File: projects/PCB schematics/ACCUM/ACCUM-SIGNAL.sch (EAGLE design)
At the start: 31 parts, among them IC1 OPA454, J1 2P_1-770166-0, J2 2P_1-770166-0, J3 2P_1-770166-0, J4 2P_1-770166-0, Q1 IRLZ44Z, X1 5566-2

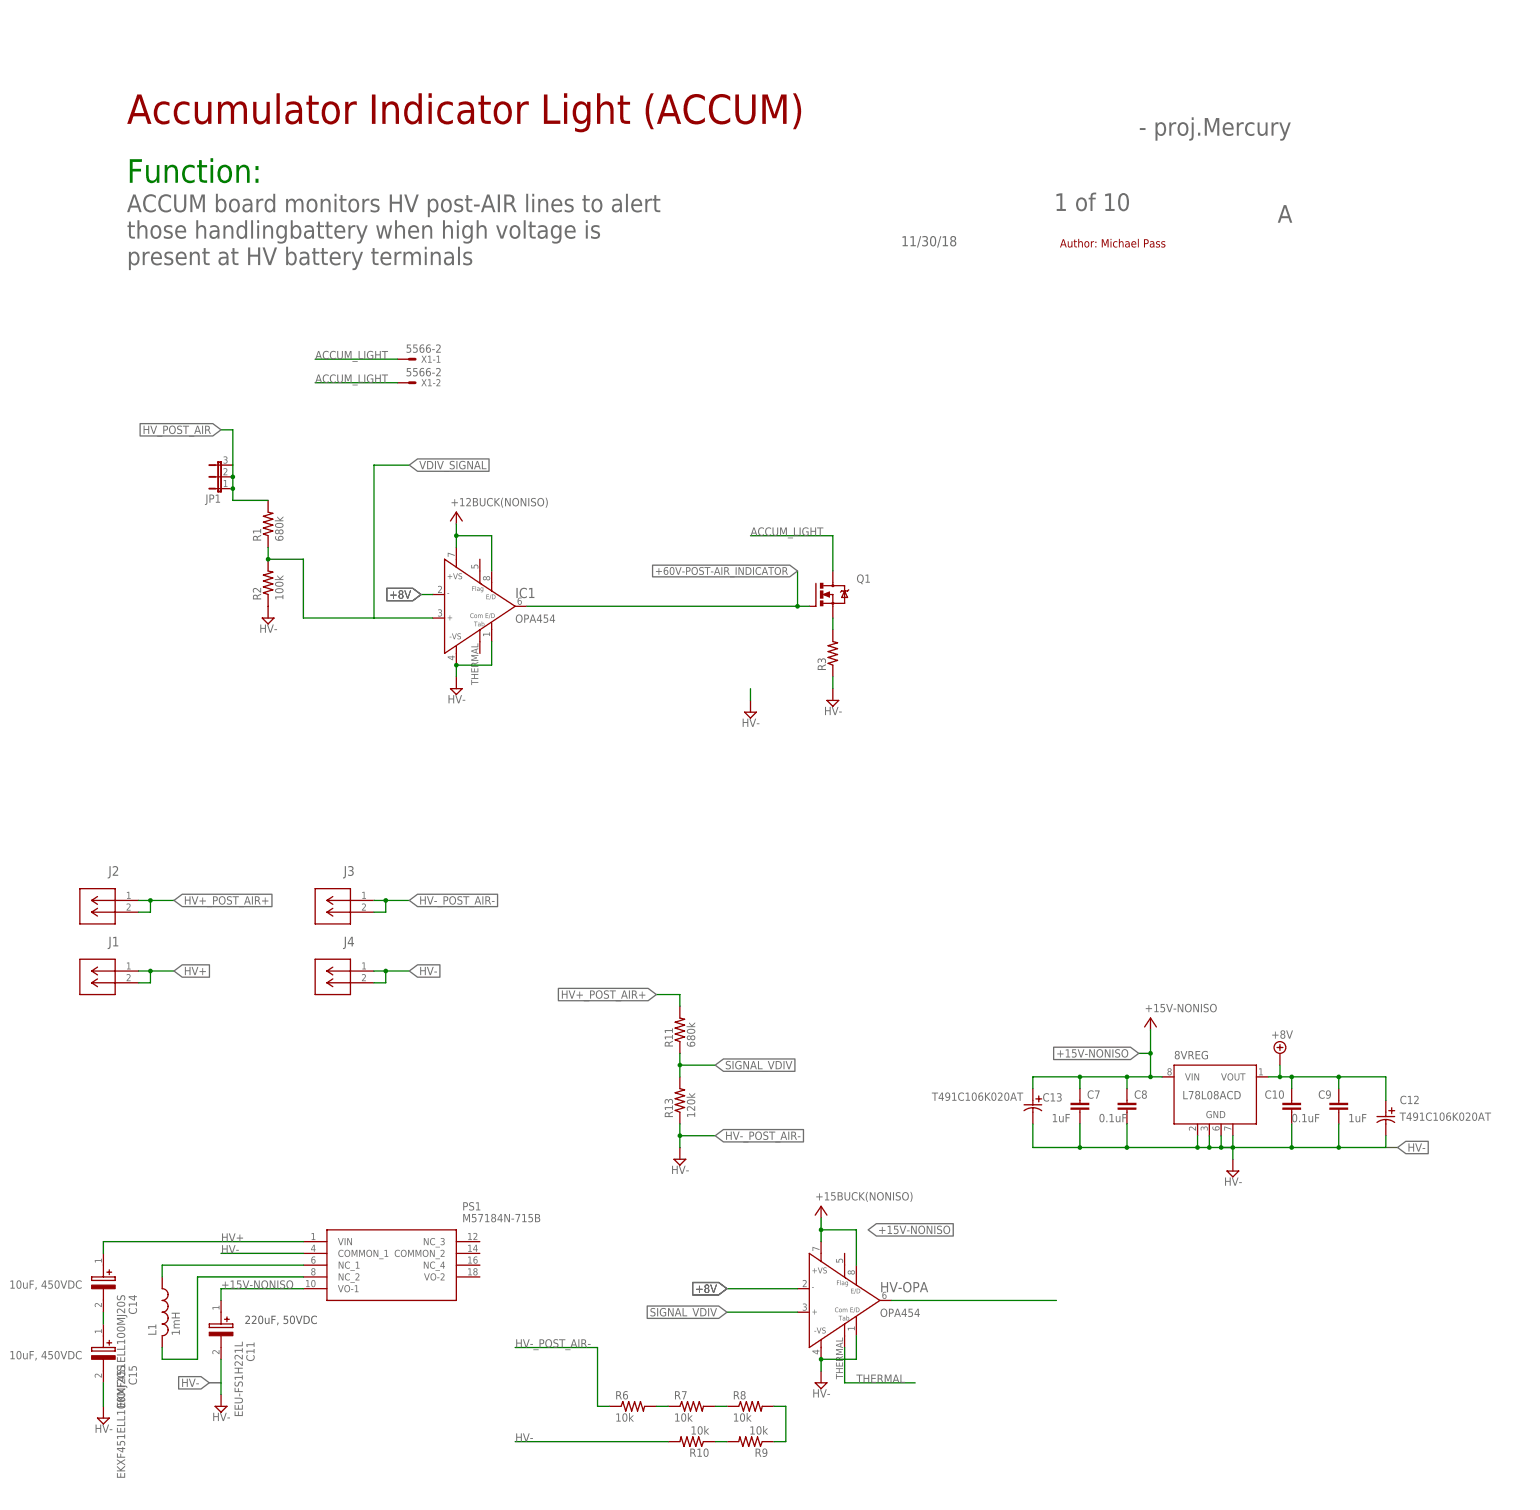
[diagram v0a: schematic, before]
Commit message: ACCUM - Added POWER board.
ACCUM - POWER and SIGNAL complete.

Two separate boards have been created. One for Powerex, and one for signal sampling.
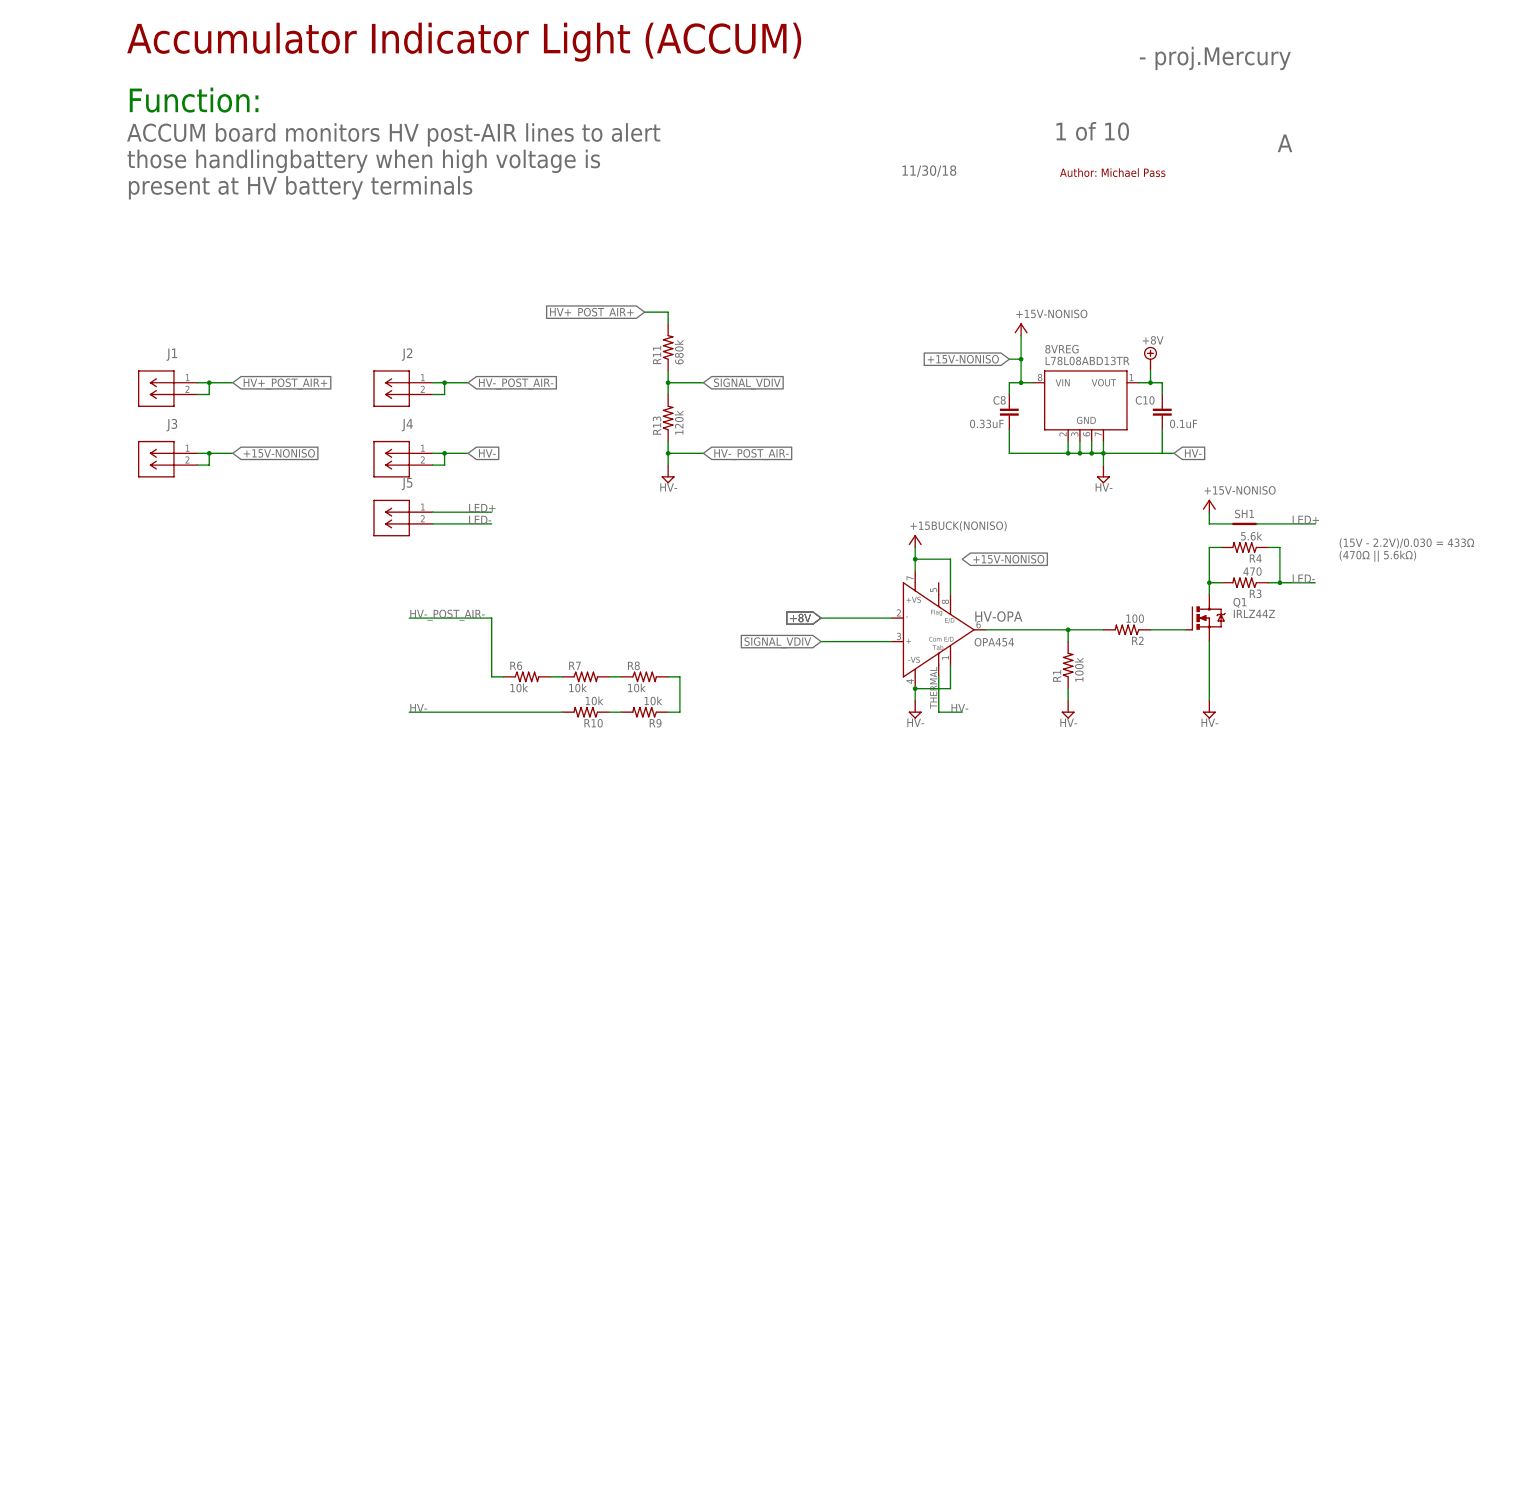
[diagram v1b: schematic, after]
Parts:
- removed C11: EEU-FS1H221L, EEU-FS1H221L:EEU-FS1H221L
- removed C12, C13: T491C106K020AT, T491C106K020AT:T491C106K020AT
- removed C14, C15: EKXF451ELL100MJ20S, EKXF451ELL100MJ20S:EKXF451ELL100MJ20S
- removed C7, C9: 1uF, rcl:C-EUC0805
- removed IC1: OPA454, OPA454:OPA454
- removed JP1: (no value), jumper:JP2W
- removed L1: 1mH, rcl:L-USL2012C
- removed PS1: M57184N-715B, M57184N-715B:M57184N-715B
- removed X1: 5566-2, con-molex:5566-2
- added J5: 2P(90DEG)_1-770966-0, con-MATE-N-LOK:2P(90DEG)_1-770966-0
- added R4: 5.6k, rcl:R-US_R0805
- added SH1: SHORTT5, shorts:SHORTT5
- 8VREG: value L78L08ACD -> L78L08ABD13TR
- C8: value 0.1uF -> 0.33uF
- J1, J2, J3, J4: value 2P_1-770166-0 -> 2P(90DEG)_1-770966-0; device con-MATE-N-LOK:2P_1-770166-0 -> con-MATE-N-LOK:2P(90DEG)_1-770966-0
- R1: value 680k -> 100k
- R2: value 100k -> 100
- R3: value (none) -> 470
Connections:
- removed net +60V-POST-AIR_INDICATOR: IC1.OUT, Q1.G
- removed net ACCUM_LIGHT: Q1.D, X1-1.S, X1-2.S
- removed net GND: R2.1, R3.1
- removed net HV+: C14.+, J1.1, J1.2, PS1.VIN
- removed net HV_POST_AIR: JP1.1, JP1.2, JP1.3, R1.2
- removed net N$2: L1.1, PS1.NC_1
- removed net N$6: Q1.S, R3.2
- removed net THERMAL: HV-OPA.E/DCOM1
- removed net V+: IC1.+VS, IC1.E/D
- removed net VDIV_SIGNAL: IC1.IN+, R1.1, R2.2
- new net LED+: J5.1, SH1.P$2
- new net LED-: J5.2, R3.1, R4.1
- net +15V-NONISO: now also J3.1, J3.2, SH1.P$1; no longer C11.+, C13.1, C7.1, PS1.VO-1
- net +8V: no longer C12.1, C9.1, IC1.IN-
- net HV+_POST_AIR+: now also J1.1, J1.2; no longer J2.1, J2.2
- net HV-: now also HV-OPA.E/DCOM1, Q1.S, R1.1; no longer C11.-, C12.2, C13.2, C15.-, C7.2, C9.2, IC1.-VS, IC1.E/DCOM, PS1.COMMON_1
- net HV-_POST_AIR-: now also J2.1, J2.2; no longer J3.1, J3.2
- net N$1: now also Q1.D, R3.2, R4.2; no longer L1.2, PS1.NC_2
- net N$3: now also Q1.G, R2.1; no longer C14.-, C15.+
- net N$9: now also R1.2, R2.2
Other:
- note added: "(15V - 2.2V)/0.030 = 433Ω (470Ω || 5.6kΩ)"
- note removed: "10uF, 450VDC"
- note removed: "220uF, 50VDC"
- moved on the sheet: 8VREG, C10, C8, HV-OPA, J1, J2, J3, J4, Q1, R1, R10, R11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

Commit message: ACCUM - BOM Created (Signal)
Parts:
- Q1: value IRLZ44Z -> IRFZ44Z
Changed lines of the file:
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@@
 <part name="R1" library="rcl" library_urn="urn:adsk.eagle:library:334" deviceset="R-US_" device="R0805" package3d_urn="urn:adsk.eagle:package:23553/2" value="100k"/>
 <part name="R2" library="rcl" library_urn="urn:adsk.eagle:library:334" deviceset="R-US_" device="R0805" package3d_urn="urn:adsk.eagle:package:23553/2" value="100"/>
-<part name="Q1" library="transistor-power" library_urn="urn:adsk.eagle:library:400" deviceset="IRLZ44Z" device="" package3d_urn="urn:adsk.eagle:package:29490/1"/>
+<part name="Q1" library="transistor-power" library_urn="urn:adsk.eagle:library:400" deviceset="IRLZ44Z" device="" package3d_urn="urn:adsk.eagle:package:29490/1" value="IRFZ44Z"/>
 <part name="SUPPLY1" library="supply2" library_urn="urn:adsk.eagle:library:372" deviceset="V+" device="" value="+15V-NONISO"/>
 <part name="SUPPLY2" library="supply2" library_urn="urn:adsk.eagle:library:372" deviceset="GND" device="" value="HV-"/>

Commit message: TEMP - Initial board placement.
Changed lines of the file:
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@@
 <part name="R11" library="rcl" library_urn="urn:adsk.eagle:library:334" deviceset="R-US_" device="R0805" package3d_urn="urn:adsk.eagle:package:23553/2" value="680k"/>
 <part name="R13" library="rcl" library_urn="urn:adsk.eagle:library:334" deviceset="R-US_" device="R0805" package3d_urn="urn:adsk.eagle:package:23553/2" value="120k"/>
-<part name="SUPPLY11" library="supply2" library_urn="urn:adsk.eagle:library:372" deviceset="GND" device="" value="HV-"/>
 <part name="R6" library="rcl" library_urn="urn:adsk.eagle:library:334" deviceset="R-US_" device="R0805" package3d_urn="urn:adsk.eagle:package:23553/2" value="10k"/>
 <part name="R7" library="rcl" library_urn="urn:adsk.eagle:library:334" deviceset="R-US_" device="R0805" package3d_urn="urn:adsk.eagle:package:23553/2" value="10k"/>
@@
 <attribute name="VALUE" x="130.302" y="80.01" size="1.778" layer="96" rot="R90"/>
 </instance>
-<instance part="SUPPLY11" gate="GND" x="127" y="71.12" smashed="yes">
-<attribute name="VALUE" x="125.095" y="67.945" size="1.778" layer="96"/>
-</instance>
 <instance part="R6" gate="G$1" x="96.52" y="27.94" smashed="yes">
 <attribute name="NAME" x="92.71" y="29.4386" size="1.778" layer="95"/>
@@
 </segment>
 <segment>
-<pinref part="SUPPLY11" gate="GND" pin="GND"/>
 <pinref part="R13" gate="G$1" pin="1"/>
 <wire x1="127" y1="73.66" x2="127" y2="76.2" width="0.1524" layer="91"/>

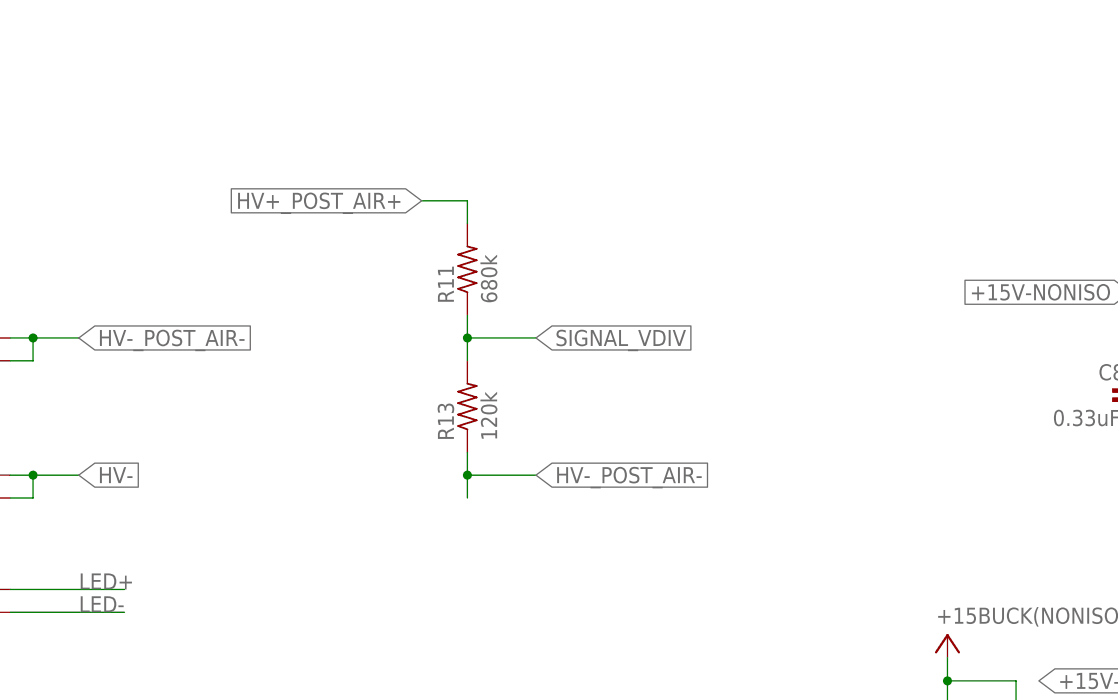
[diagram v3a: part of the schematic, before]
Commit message: TSAL - Added in fuses.
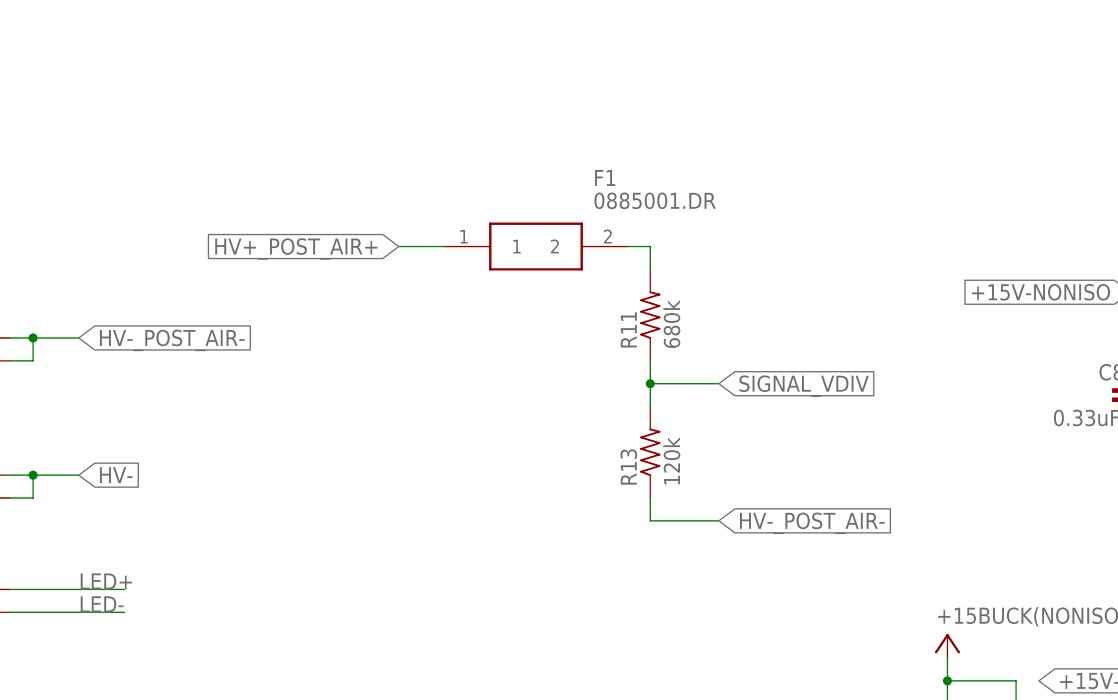
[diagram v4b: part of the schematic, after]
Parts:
- added F1: 0885001.DR, 0885001.DR:0885001.DR
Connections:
- new net N$2: F1.2, R11.2
- net HV+_POST_AIR+: now also F1.1; no longer R11.2
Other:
- moved on the sheet: R11, R13
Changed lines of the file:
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@@
 <?xml version="1.0" encoding="utf-8"?>
 <!DOCTYPE eagle SYSTEM "eagle.dtd">
-<eagle version="9.3.2">
+<eagle version="9.4.0">
 <drawing>
 <settings>
@@
 <part name="SUPPLY3" library="supply2" library_urn="urn:adsk.eagle:library:372" deviceset="GND" device="" value="HV-"/>
 <part name="R4" library="rcl" library_urn="urn:adsk.eagle:library:334" deviceset="R-US_" device="R0805" package3d_urn="urn:adsk.eagle:package:23553/2" value="5.6k"/>
+<part name="F1" library="0885001.DR" deviceset="0885001.DR" device=""/>
 </parts>
 <sheets>
@@
 <attribute name="VALUE" x="178.435" y="17.145" size="1.778" layer="96"/>
 </instance>
-<instance part="R11" gate="G$1" x="127" y="99.06" smashed="yes" rot="R90">
-<attribute name="NAME" x="125.5014" y="95.25" size="1.778" layer="95" rot="R90"/>
-<attribute name="VALUE" x="130.302" y="95.25" size="1.778" layer="96" rot="R90"/>
-</instance>
-<instance part="R13" gate="G$1" x="127" y="83.82" smashed="yes" rot="R90">
-<attribute name="NAME" x="125.5014" y="80.01" size="1.778" layer="95" rot="R90"/>
-<attribute name="VALUE" x="130.302" y="80.01" size="1.778" layer="96" rot="R90"/>
+<instance part="R11" gate="G$1" x="147.32" y="93.98" smashed="yes" rot="R90">
+<attribute name="NAME" x="145.8214" y="90.17" size="1.778" layer="95" rot="R90"/>
+<attribute name="VALUE" x="150.622" y="90.17" size="1.778" layer="96" rot="R90"/>
+</instance>
+<instance part="R13" gate="G$1" x="147.32" y="78.74" smashed="yes" rot="R90">
+<attribute name="NAME" x="145.8214" y="74.93" size="1.778" layer="95" rot="R90"/>
+<attribute name="VALUE" x="150.622" y="74.93" size="1.778" layer="96" rot="R90"/>
 </instance>
 <instance part="R6" gate="G$1" x="96.52" y="27.94" smashed="yes">
@@
 <attribute name="NAME" x="255.27" y="54.3814" size="1.778" layer="95" rot="R180"/>
 <attribute name="VALUE" x="255.27" y="59.182" size="1.778" layer="96" rot="R180"/>
+</instance>
+<instance part="F1" gate="G$1" x="124.46" y="101.6" smashed="yes">
+<attribute name="NAME" x="140.97" y="109.22" size="1.778" layer="95" align="center-left"/>
+<attribute name="VALUE" x="140.97" y="106.68" size="1.778" layer="96" align="center-left"/>
 </instance>
 </instances>
@@
 <segment>
 <pinref part="R13" gate="G$1" pin="2"/>
-<wire x1="127" y1="88.9" x2="127" y2="91.44" width="0.1524" layer="91"/>
-<label x="134.62" y="91.44" size="1.778" layer="95" xref="yes"/>
+<wire x1="147.32" y1="83.82" x2="147.32" y2="86.36" width="0.1524" layer="91"/>
+<label x="154.94" y="86.36" size="1.778" layer="95" xref="yes"/>
 <pinref part="R11" gate="G$1" pin="1"/>
-<wire x1="127" y1="91.44" x2="127" y2="93.98" width="0.1524" layer="91"/>
-<wire x1="127" y1="91.44" x2="134.62" y2="91.44" width="0.1524" layer="91"/>
-<junction x="127" y="91.44"/>
+<wire x1="147.32" y1="86.36" x2="147.32" y2="88.9" width="0.1524" layer="91"/>
+<wire x1="147.32" y1="86.36" x2="154.94" y2="86.36" width="0.1524" layer="91"/>
+<junction x="147.32" y="86.36"/>
 </segment>
 </net>
@@
 </segment>
 <segment>
-<wire x1="121.92" y1="106.68" x2="127" y2="106.68" width="0.1524" layer="91"/>
-<wire x1="127" y1="106.68" x2="127" y2="104.14" width="0.1524" layer="91"/>
-<pinref part="R11" gate="G$1" pin="2"/>
-<label x="121.92" y="106.68" size="1.778" layer="95" rot="R180" xref="yes"/>
+<wire x1="119.38" y1="101.6" x2="124.46" y2="101.6" width="0.1524" layer="91"/>
+<label x="119.38" y="101.6" size="1.778" layer="95" rot="R180" xref="yes"/>
+<pinref part="F1" gate="G$1" pin="1"/>
 </segment>
 </net>
@@
 <segment>
 <pinref part="R13" gate="G$1" pin="1"/>
-<wire x1="127" y1="73.66" x2="127" y2="76.2" width="0.1524" layer="91"/>
-<label x="134.62" y="76.2" size="1.778" layer="95" xref="yes"/>
-<wire x1="127" y1="76.2" x2="127" y2="78.74" width="0.1524" layer="91"/>
-<wire x1="127" y1="76.2" x2="134.62" y2="76.2" width="0.1524" layer="91"/>
-<junction x="127" y="76.2"/>
+<label x="154.94" y="71.12" size="1.778" layer="95" xref="yes"/>
+<wire x1="147.32" y1="71.12" x2="147.32" y2="73.66" width="0.1524" layer="91"/>
+<wire x1="147.32" y1="71.12" x2="154.94" y2="71.12" width="0.1524" layer="91"/>
 </segment>
 <segment>
@@
 </segment>
 </net>
+<net name="N$2" class="0">
+<segment>
+<pinref part="F1" gate="G$1" pin="2"/>
+<wire x1="144.78" y1="101.6" x2="147.32" y2="101.6" width="0.1524" layer="91"/>
+<pinref part="R11" gate="G$1" pin="2"/>
+<wire x1="147.32" y1="101.6" x2="147.32" y2="99.06" width="0.1524" layer="91"/>
+</segment>
+</net>
